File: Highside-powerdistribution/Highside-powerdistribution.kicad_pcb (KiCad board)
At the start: 2 copper layers, 100 x 100 mm, 54 parts, among them J1 Conn_01x02_Male, J10 Screw_Terminal_01x02, J11 Screw_Terminal_01x02, J12 Screw_Terminal_01x02, J13 Screw_Terminal_01x02, J14 Conn_01x02, J15 Screw_Terminal_01x06, J2 Conn_01x02_Male, J3 Conn_01x02_Male, J4 Conn_01x02_Male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

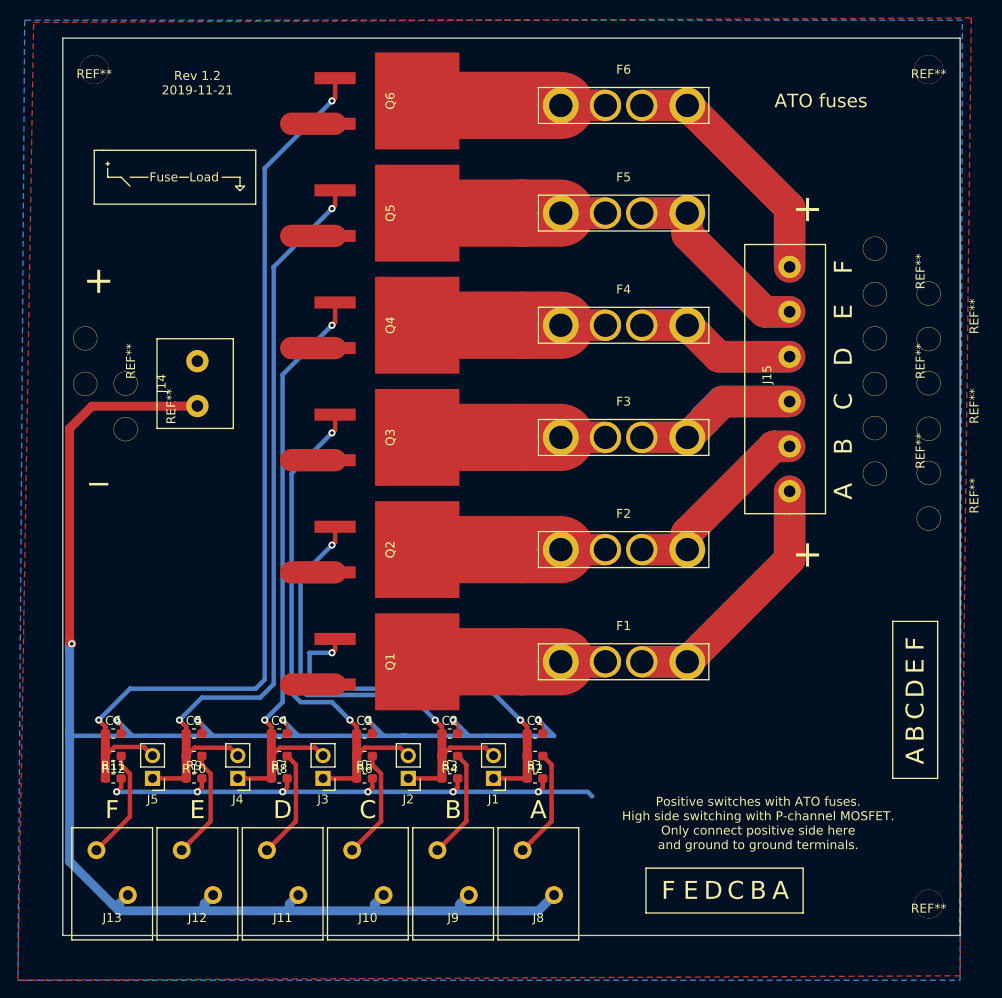
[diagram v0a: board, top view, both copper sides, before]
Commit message: Better copper management
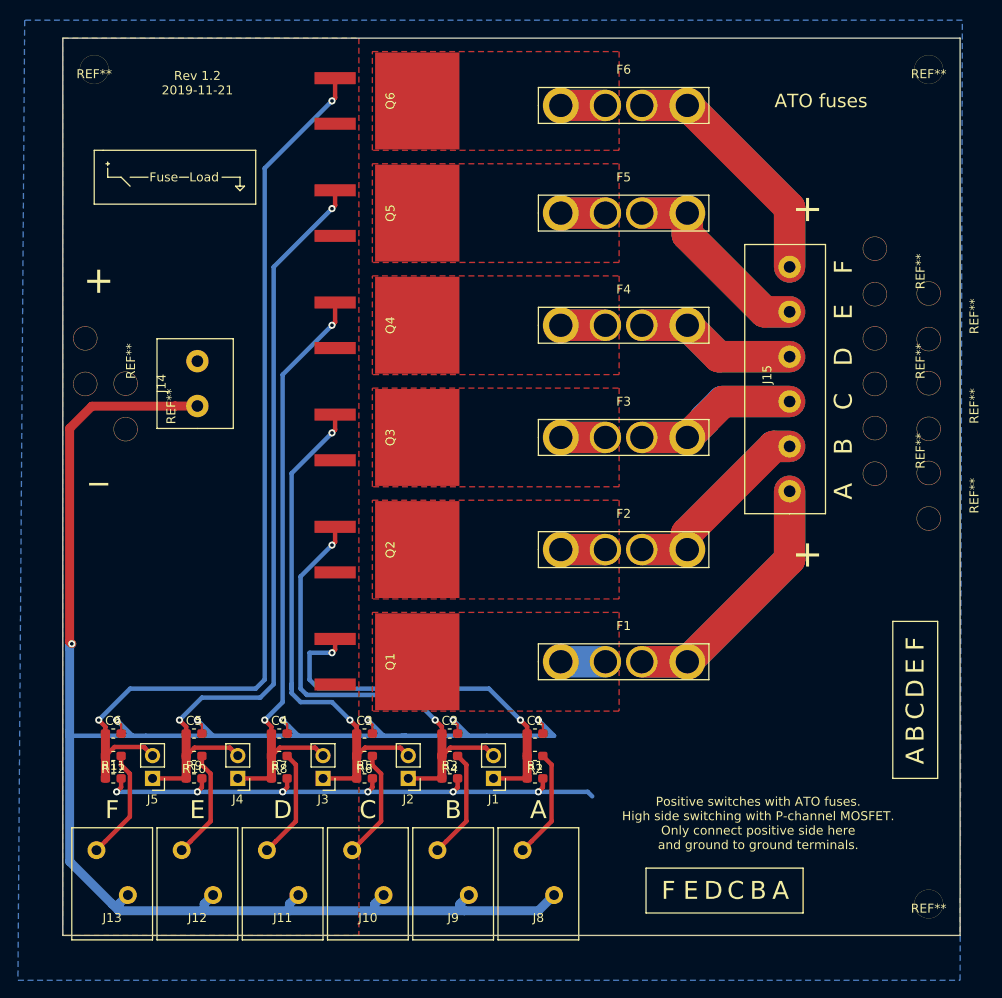
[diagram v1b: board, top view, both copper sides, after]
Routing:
- net +12V: track 92.8 -> 63.4 mm
- net SSR-A: track 25.9 -> 4.97 mm
- net SSR-F: track 26.1 -> 9.94 mm
- net SSR-E: track 25.9 -> 9.94 mm
- net SSR-D: track 25.9 -> 9.94 mm
- net SSR-C: track 25.9 -> 9.94 mm
- net SSR-B: track 25.9 -> 9.94 mm
- added copper zone on F.Cu, net SSR-A
- added copper zone on F.Cu, net SSR-B
- added copper zone on F.Cu, net SSR-C
- added copper zone on F.Cu, net SSR-D
- added copper zone on F.Cu, net SSR-E
- added copper zone on F.Cu, net SSR-F
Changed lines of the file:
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@@
     (thickness 1.6)
     (drawings 63)
-    (tracks 293)
+    (tracks 274)
     (zones 0)
     (modules 54)
@@
   (gr_line (start 150 150) (end 150 50) (layer Edge.Cuts) (width 0.12))
   (gr_line (start 50 150) (end 150 150) (layer Edge.Cuts) (width 0.12))
-  (segment (start 80.35 59.54) (end 75.46 59.54) (width 2.5) (layer F.Cu) (net 1))
-  (segment (start 80.35 72.04) (end 75.46 72.04) (width 2.5) (layer F.Cu) (net 1))
-  (segment (start 80.35 84.54) (end 75.46 84.54) (width 2.5) (layer F.Cu) (net 1))
-  (segment (start 80.35 97.04) (end 75.46 97.04) (width 2.5) (layer F.Cu) (net 1))
-  (segment (start 80.35 109.54) (end 75.46 109.54) (width 2.5) (layer F.Cu) (net 1))
-  (segment (start 80.35 122.04) (end 75.46 122.04) (width 2.5) (layer F.Cu) (net 1))
   (via (at 103 134) (size 0.8) (drill 0.4) (layers F.Cu B.Cu) (net 1))
   (segment (start 103.5 132.5) (end 103.5 133.5) (width 0.5) (layer F.Cu) (net 1))
@@
   (segment (start 51 117.5) (end 50.76001 117.26001) (width 1) (layer F.Cu) (net 2))
   (segment (start 50.76001 117.26001) (end 50.76001 93.5) (width 1) (layer F.Cu) (net 2))
-  (segment (start 101.2 119.5) (end 89.5 119.5) (width 7.5) (layer F.Cu) (net 3))
-  (segment (start 105.5 119.5) (end 101.2 119.5) (width 7.5) (layer F.Cu) (net 3))
-  (segment (start 105.5 119.5) (end 110.47 119.5) (width 3.5) (layer F.Cu) (net 3))
   (segment (start 110.47 119.5) (end 105.5 119.5) (width 3.5) (layer B.Cu) (net 3))
-  (segment (start 101.2 107) (end 89.5 107) (width 7.5) (layer F.Cu) (net 4))
-  (segment (start 105.5 107) (end 101.2 107) (width 7.5) (layer F.Cu) (net 4))
   (segment (start 105.5 107) (end 110.47 107) (width 3.5) (layer F.Cu) (net 4))
   (segment (start 110.47 107) (end 105.5 107) (width 3.5) (layer B.Cu) (net 4))
-  (segment (start 101.2 94.5) (end 89.5 94.5) (width 7.5) (layer F.Cu) (net 5))
-  (segment (start 105.5 94.5) (end 101.2 94.5) (width 7.5) (layer F.Cu) (net 5))
   (segment (start 105.5 94.5) (end 110.47 94.5) (width 3.5) (layer F.Cu) (net 5))
   (segment (start 110.47 94.5) (end 105.5 94.5) (width 3.5) (layer B.Cu) (net 5))
-  (segment (start 101.2 82) (end 89.5 82) (width 7.5) (layer F.Cu) (net 6))
-  (segment (start 105.5 82) (end 101.2 82) (width 7.5) (layer F.Cu) (net 6))
   (segment (start 105.5 82) (end 110.47 82) (width 3.5) (layer F.Cu) (net 6))
   (segment (start 110.47 82) (end 105.5 82) (width 3.5) (layer B.Cu) (net 6))
-  (segment (start 101.2 69.5) (end 89.5 69.5) (width 7.5) (layer F.Cu) (net 7))
-  (segment (start 105.5 69.5) (end 101.2 69.5) (width 7.5) (layer F.Cu) (net 7))
   (segment (start 105.5 69.5) (end 110.47 69.5) (width 3.5) (layer F.Cu) (net 7))
   (segment (start 110.47 69.5) (end 105.5 69.5) (width 3.5) (layer B.Cu) (net 7))
-  (segment (start 90 57.5) (end 89.5 57) (width 7.5) (layer F.Cu) (net 8))
-  (segment (start 105.5 57.5) (end 90 57.5) (width 7.5) (layer F.Cu) (net 8))
   (segment (start 110.47 57.5) (end 105.5 57.5) (width 3.5) (layer F.Cu) (net 8))
   (segment (start 105.5 57.5) (end 110.47 57.5) (width 3.5) (layer B.Cu) (net 8))
@@
   (segment (start 56.5 130) (end 56.5 131.002712) (width 0.5) (layer F.Cu) (net 26))
   (zone (net 1) (net_name +12V) (layer B.Cu) (hatch edge 0.508)
-    (connect_pads (clearance 0.508))
+    (connect_pads yes (clearance 0.508))
     (min_thickness 0.254)
     (fill yes (arc_segments 32) (thermal_gap 0.508) (thermal_bridge_width 0.508))
@@
   )
   (zone (net 1) (net_name +12V) (layer F.Cu) (hatch edge 0.508)
-    (connect_pads (clearance 0.508))
+    (connect_pads yes (clearance 0.508))
     (min_thickness 0.254)
     (fill yes (arc_segments 32) (thermal_gap 0.508) (thermal_bridge_width 0.508))
     (polygon
       (pts
-        (xy 46.75 48.25) (xy 151.25 47.75) (xy 150 154.5) (xy 45 155)
+        (xy 50 50) (xy 83 50) (xy 83 150) (xy 50 150)
       )
     )
@@
       )
     )
+  )
+  (zone (net 3) (net_name SSR-A) (layer F.Cu) (hatch edge 0.508)
+    (connect_pads yes (clearance 0.508))
+    (min_thickness 0.254)
+    (fill yes (arc_segments 32) (thermal_gap 0.508) (thermal_bridge_width 0.508))
+    (polygon
+      (pts
+        (xy 84.5 114) (xy 112 114) (xy 112 125) (xy 84.5 125)
+      )
+    )
+  )
+  (zone (net 4) (net_name SSR-B) (layer F.Cu) (hatch edge 0.508)
+    (connect_pads yes (clearance 0.508))
+    (min_thickness 0.254)
+    (fill yes (arc_segments 32) (thermal_gap 0.508) (thermal_bridge_width 0.508))
+    (polygon
+      (pts
+        (xy 84.5 101.5) (xy 112 101.5) (xy 112 112.5) (xy 84.5 112.5)
+      )
+    )
+  )
+  (zone (net 5) (net_name SSR-C) (layer F.Cu) (hatch edge 0.508)
+    (connect_pads yes (clearance 0.508))
+    (min_thickness 0.254)
+    (fill yes (arc_segments 32) (thermal_gap 0.508) (thermal_bridge_width 0.508))
+    (polygon
+      (pts
+        (xy 84.5 89) (xy 112 89) (xy 112 100) (xy 84.5 100)
+      )
+    )
+  )
+  (zone (net 6) (net_name SSR-D) (layer F.Cu) (hatch edge 0.508)
+    (connect_pads yes (clearance 0.508))
+    (min_thickness 0.254)
+    (fill yes (arc_segments 32) (thermal_gap 0.508) (thermal_bridge_width 0.508))
+    (polygon
+      (pts
+        (xy 84.5 76.5) (xy 112 76.5) (xy 112 87.5) (xy 84.5 87.5)
+      )
+    )
+  )
+  (zone (net 7) (net_name SSR-E) (layer F.Cu) (hatch edge 0.508)
+    (connect_pads yes (clearance 0.508))
+    (min_thickness 0.254)
+    (fill yes (arc_segments 32) (thermal_gap 0.508) (thermal_bridge_width 0.508))
+    (polygon
+      (pts
+        (xy 84.5 64) (xy 112 64) (xy 112 75) (xy 84.5 75)
+      )
+    )
+  )
+  (zone (net 8) (net_name SSR-F) (layer F.Cu) (hatch edge 0.508)
+    (connect_pads yes (clearance 0.508))
+    (min_thickness 0.254)
+    (fill yes (arc_segments 32) (thermal_gap 0.508) (thermal_bridge_width 0.508))
+    (polygon
+      (pts
+        (xy 84.5 51.5) (xy 112 51.5) (xy 112 62.5) (xy 84.5 62.5)
+      )
+    )

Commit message: Update Highside-powerdistribution.kicad_pcb
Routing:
- net GND: track 211.3 -> 212.2 mm, vias 7 -> 6
- net SSR-F: vias 0 -> 25
- net SSR-E: vias 0 -> 25
- net SSR-D: vias 0 -> 25
- net SSR-C: vias 0 -> 25
- net SSR-B: vias 0 -> 25
- net SSR-A: vias 0 -> 25
- net +12V: vias 6 -> 22
- added copper zone on B.Cu, net Net-(F3-Pad1)
- added copper zone on F.Cu, net Net-(F3-Pad1)
- added copper zone on B.Cu, net Net-(F4-Pad1)
- added copper zone on F.Cu, net Net-(F4-Pad1)
- added copper zone on B.Cu, net SSR-A
- added copper zone on B.Cu, net SSR-B
- added copper zone on B.Cu, net SSR-C
- added copper zone on B.Cu, net SSR-D
- added copper zone on B.Cu, net SSR-E
- added copper zone on B.Cu, net SSR-F
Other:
- board text added: "Rev 1.3 2020-01-08"
- board text removed: "Rev 1.2 2019-11-21"

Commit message: Moved filled zone to remove shortcurcit
12V and the mosfets had filled zone together
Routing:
- net +12V: track 63.4 -> 74.9 mm
